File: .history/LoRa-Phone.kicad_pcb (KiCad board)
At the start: 4 copper layers, 60 x 102.5 mm, 188 parts, among them IC1 SKY13373-460LF, IC2 AD8318ACPZ-REEL7, IC3 AD8318ACPZ-REEL7, IC4 TPS2121RUXT, IC5 MAX17048G+T10, IC6 MAX17048G+T10, IC7 TCA9543ADR, IC8 MAX16150AUT+T, J1 Interface, J2 Connector, J3 Connector, J4 BUTTON, J4 JST_MAIN, J6 ROTARY_ENCODER, M1 Motor_DC, Q1 AO3400A, Q4 AO3401A, SW1 POWER, U1 ESP32-S3-WROOM-2, U10 DRV2605LDGS, U11 LC76G, U12 RV-3028-C7, U13 SA818S, U14 INA219BxDCN, U15 INA219BxDCN, U16 INA219BxDCN, U2 TCD-10-23BDX+, U21 WM8960, U23 E22-900M30S, U24 E22-170M30S, U3 MCP23017x-x-ML, U4 BMP390, U5 IS31FL3218-QF, U6 LSM6DSOXTR, U7 BQ24075RGT, U8 MCP23017x-x-ML, U9 BQ24075RGT

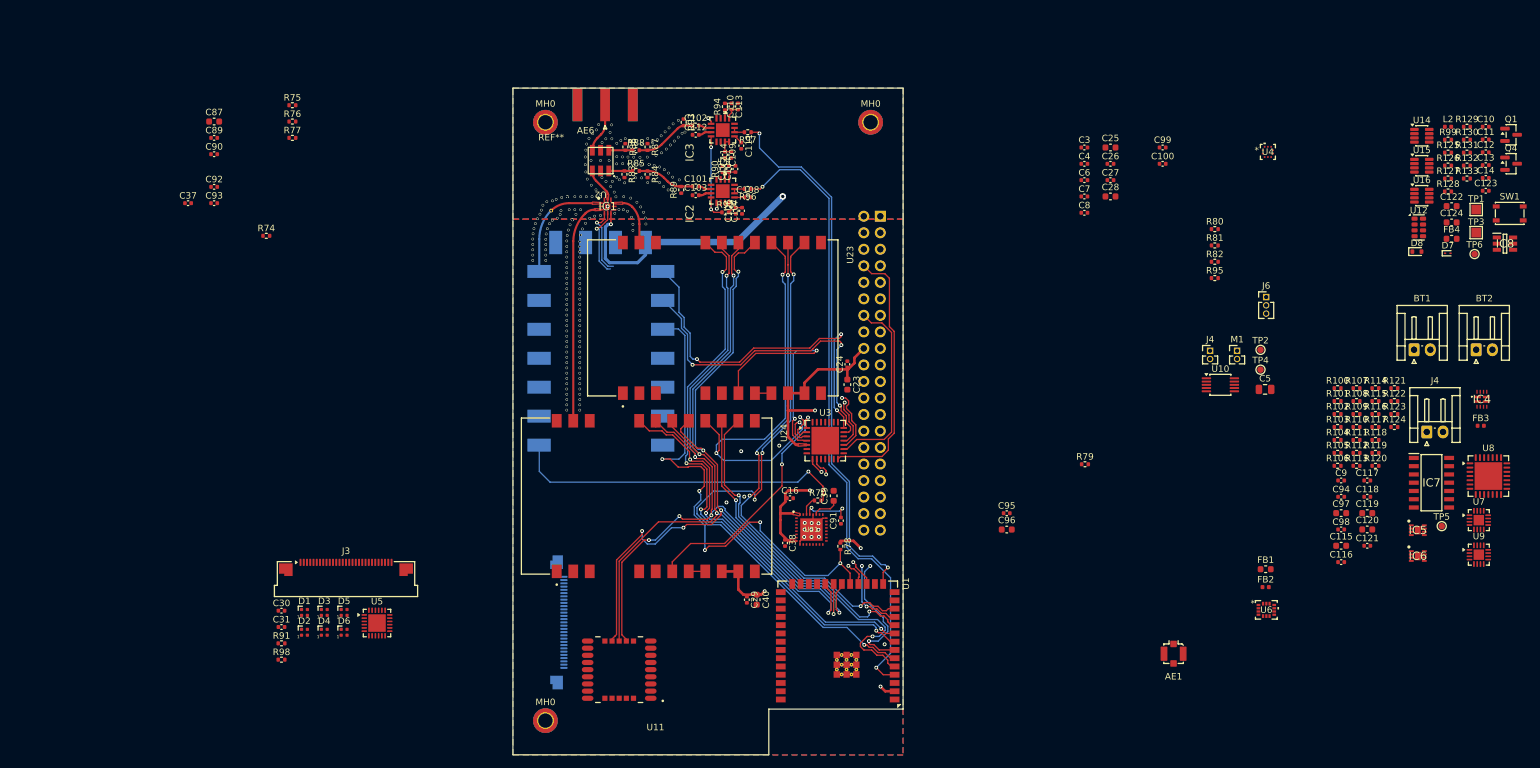
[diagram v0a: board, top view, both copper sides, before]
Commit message: Routed secondary PCB with Power and charging managment, and routed FPC Connector
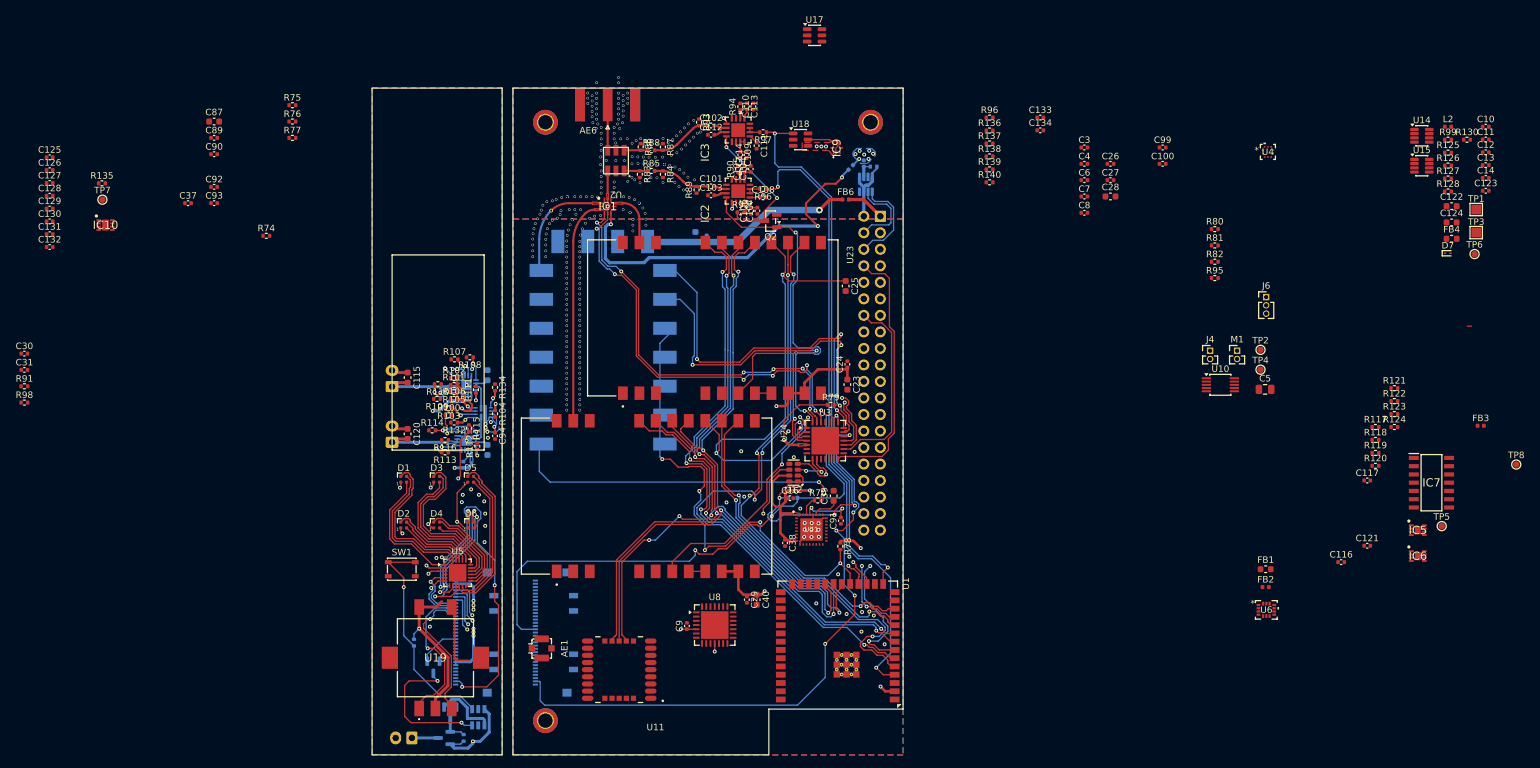
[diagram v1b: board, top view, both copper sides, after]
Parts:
- removed J2: Connector, Connector_FFC-FPC:Amphenol_F32R-1A7x1-11029_1x29-1MP_P0.5mm_Horizontal
- added C125: 100nF, Capacitor_SMD:C_0402_1005Metric, F.Cu at (45.4, 61.9)
- added C126: 2.2uF, Capacitor_SMD:C_0402_1005Metric, F.Cu at (45.4, 63.9)
- added C127: 2.2uF, Capacitor_SMD:C_0402_1005Metric, F.Cu at (45.4, 65.8)
- added C128: 100nF, Capacitor_SMD:C_0402_1005Metric, F.Cu at (45.4, 67.8)
- added C129: 2.2uF, Capacitor_SMD:C_0402_1005Metric, F.Cu at (45.4, 69.8)
- added C130: 100nF, Capacitor_SMD:C_0402_1005Metric, F.Cu at (45.4, 71.7)
- added C131: 100nF, Capacitor_SMD:C_0402_1005Metric, F.Cu at (45.4, 73.7)
- added C132: 100nF, Capacitor_SMD:C_0402_1005Metric, F.Cu at (45.4, 75.7)
- added C133: 100nF, Capacitor_SMD:C_0402_1005Metric, F.Cu at (197.7, 55.8)
- added C134: 100nF, Capacitor_SMD:C_0402_1005Metric, F.Cu at (197.7, 57.7)
- added FB5: 600R @100MHz 500mA, Inductor_SMD:L_0402_1005Metric, B.Cu at (168.5, 63.4)
- added FB6: 600R @100MHz 500mA, Inductor_SMD:L_0402_1005Metric, F.Cu at (167.8, 68.4)
- added FB7: 600R @100MHz 4A, Inductor_SMD:L_0402_1005Metric, B.Cu at (170.6, 62.8)
- added IC10: TPS22965NTDSGRQ1, PTCR:SON50P200X200X80-9N, F.Cu at (54.0, 72.3)
- added IC9: SN74LVC1G74RSE2, PTCR:SN74LVC1G74RSE2, F.Cu at (166.4, 60.4)
- added J5: Board_1, Connector_FFC-FPC:Molex_502244-3330_1x33-1MP_P0.5mm_Horizontal, B.Cu at (110.9, 135.0)
- added Q2: AO3400A, Package_TO_SOT_SMD:SOT-23, F.Cu at (156.2, 71.7)
- added Q3: AO3400A, Package_TO_SOT_SMD:SOT-23, B.Cu at (104.4, 140.3)
- added R134: 5K, Resistor_SMD:R_0402_1005Metric, F.Cu at (113.8, 97.3)
- added R135: 1K, Resistor_SMD:R_0402_1005Metric, F.Cu at (53.4, 65.9)
- added R136: 10K 0.1%, Resistor_SMD:R_0402_1005Metric, F.Cu at (189.9, 57.8)
- added R137: 5.6K 0.1%, Resistor_SMD:R_0402_1005Metric, F.Cu at (189.9, 59.8)
- added R138: 10K 0.1%, Resistor_SMD:R_0402_1005Metric, F.Cu at (189.9, 61.8)
- added R139: 10K, Resistor_SMD:R_0402_1005Metric, F.Cu at (189.9, 63.7)
- added R140: 10K, Resistor_SMD:R_0402_1005Metric, F.Cu at (189.9, 65.7)
- added R96: 10K, Resistor_SMD:R_0402_1005Metric, F.Cu at (189.9, 55.8)
- added TP7: +3V3_RF, TestPoint:TestPoint_Pad_D1.0mm, F.Cu at (53.5, 68.4)
- added TP8: +5V_RF, TestPoint:TestPoint_Pad_D1.0mm, F.Cu at (270.9, 109.1)
- added U17: MCP4725xxx-xCH, Package_TO_SOT_SMD:SOT-23-6, F.Cu at (163.0, 43.1)
- added U18: TLV3501AIDBV, Package_TO_SOT_SMD:SOT-23-6, F.Cu at (160.8, 59.2)
- added U19: RIC11-31S10K2-GSMT, PTCR:RIC1131S10K2GSMT, F.Cu at (104.7, 138.8)
- BT1, BT2, C118, C119, C95, C96, C97, C98, D8, IC4, IC8, J4, Q1, Q4, R129, R131, U16, U7, U9: moved to B.Cu
- FB1: value 600R @100MHz 1A -> 600R @100MHz 2A
- J3: value Connector -> Board_1; footprint Connector_FFC-FPC:Amphenol_F32R-1A7x1-11029_1x29-1MP_P0.5mm_Horizontal -> Connector_FFC-FPC:Molex_502244-3330_1x33-1MP_P0.5mm_Horizontal; moved to B.Cu
- R100: value 13.7K -> 16K
- R101: value 23.7K -> 16K
- R133: value 51.1K -> 100K; moved to B.Cu
- R97: value 1K -> 5.6K 0.1%
- TP5: value +3V3_RF -> +5V_RF
- moved Q4 186.3 mm to (106.0, 151.2), turned to 180 degrees
- moved Q1 185.8 mm to (107.0, 147.4), turned to -90 degrees
- moved R129 180.3 mm to (101.4, 136.5), turned to 90 degrees
- moved SW1 178.9 mm to (99.5, 125.2)
- moved R133 176.6 mm to (109.0, 151.2), turned to -90 degrees
- moved IC8 173.8 mm to (111.3, 148.0), turned to -90 degrees
- moved BT2 167.3 mm to (98.0, 105.7), turned to 90 degrees
- moved J4 163.0 mm to (101.1, 151.2), turned to 180 degrees
- moved R132 160.6 mm to (107.6, 102.7), turned to 180 degrees
- moved BT1 157.2 mm to (98.0, 97.2), turned to 90 degrees
- moved U7 157.0 mm to (109.5, 96.9)
- moved U9 156.6 mm to (109.5, 105.5)
- moved IC4 153.5 mm to (112.1, 101.2), turned to 90 degrees
- moved C120 148.3 mm to (100.4, 104.4), turned to -90 degrees
- moved C115 145.8 mm to (100.4, 95.8), turned to -90 degrees
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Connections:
- C104 pad 1: +3V3_RF -> +5V_RF
- C105 pad 1: +3V3_RF -> +5V_RF
- C106 pad 2: +3V3_RF -> +5V_RF
- C107 pad 2: +3V3_RF -> +5V_RF
- C109 pad 1: +3V3_RF -> +5V_RF
- C110 pad 1: +3V3_RF -> +5V_RF
- C113 pad 2: +3V3_RF -> +5V_RF
- C114 pad 2: +3V3_RF -> +5V_RF
- C123 pad 1: SHUTDOWN -> Net-(IC8-~{CLR})
- C37 pad 1: Net-(U21-DBVDD) -> +3V3
- C95 pad 1: +3V3_RADIO -> +5V_RADIO
- C96 pad 1: +3V3_RADIO -> +5V_RADIO
- D1 pad 1: GND -> +3V3
- D2 pad 1: GND -> +3V3
- D3 pad 1: GND -> +3V3
- D4 pad 1: GND -> +3V3
- D5 pad 1: GND -> +3V3
- D6 pad 1: GND -> +3V3
- D8 pad 1: POWER_BTN -> INT_RTC
- D8 pad 2: INT_RTC -> POWER_BTN_B
- FB3 pad 1: +3V3_RF -> +5V_RF
- FB3 pad 2: +3V3 -> +5V
- IC2 pad 3: +3V3_RF -> +5V_RF
- IC2 pad 4: +3V3_RF -> +5V_RF
- IC2 pad 9: +3V3_RF -> +5V_RF
- IC3 pad 16: AD8318_EN -> Net-(IC3-ENBL)
- IC3 pad 3: +3V3_RF -> +5V_RF
- IC3 pad 4: +3V3_RF -> +5V_RF
- IC3 pad 9: +3V3_RF -> +5V_RF
- IC5 pad 7: SD0 -> SC0
- IC5 pad 8: SC0 -> SD0
- IC6 pad 7: SD1 -> SC1
- IC6 pad 8: SC1 -> SD1
- IC8 pad 1: POWER_BTN -> POWER_BTN_B
- IC8 pad 6: SHUTDOWN -> Net-(IC8-~{CLR})
- J3 pad 10: D5B -> ROT_ENC1
- J3 pad 11: D6R -> ROT_ENC2
- J3 pad 12: D6G -> JOYSTICK_X
- J3 pad 13: D6B -> JOYSTICK_Y
- J3 pad 14: GND -> BUTTON1
- J3 pad 15: GND -> BUTTON0
- J3 pad 16: ROT_ENC2_B -> POWER_BTN
- J3 pad 17: ROT_ENC1_B -> BATS_INT_1
- J3 pad 18: BUTTON0_B -> BAT_SEL_1
- J3 pad 19: D1R -> SHUTDOWN_1
- J3 pad 20: D1G -> BAT_VAL_1
- J3 pad 21: D1B -> BATS_RESET_1
- J3 pad 22: D2R -> GND
- J3 pad 23: D2G -> GND
- J3 pad 24: D2B -> GND
- J3 pad 25: D3R -> +5V
- J3 pad 26: D3G -> +5V
- J3 pad 27: D3B -> +5V
- J3 pad 28: D4R -> GND
- J3 pad 29: D4G -> GND
- J3 pad 3: BUTTON1_B -> +3V3
- J3 pad 4: JOYSTICK_Y_B -> BAT1_PGOOD_1
- J3 pad 5: JOYSTICK_X_B -> BAT1_CHG_1
- J3 pad 6: SDA -> BAT2_PGOOD_1
- J3 pad 7: SCL -> BAT2_CHG_1
- J3 pad 8: D5R -> SDA
- J3 pad 9: D5G -> SCL
- R127 pad 1: +3V3_RADIO -> +3V3_RADIO_OUT
- R128 pad 2: SHUTDOWN -> Net-(IC8-~{CLR})
- R129 pad 1: POWER_BTN -> POWER_BTN_B
- R129 pad 2: BAT_OUT -> +3V3
- R131 pad 1: +3V3 -> Net-(U16-IN-)
- R92 pad 1: AD8318_EN -> Net-(IC3-ENBL)
- R92 pad 2: +3V3_RF -> +5V_RF
- R98 pad 1: SDB -> SDB_1
- SW1 pad 1: POWER_BTN -> POWER_BTN_B
- TP5 pad 1: +3V3_RF -> +5V_RF
- U11 pad 6: BAT_OUT -> unconnected-(U11-V_BCKP-Pad6)
- U13 pad 8: +3V3_RADIO -> +5V_RADIO
- U14 pad 2: +3V3_RADIO -> +3V3_RADIO_OUT
- U16 pad 2: +3V3 -> Net-(U16-IN-)
- U21 pad 10: Net-(U21-DBVDD) -> +3V3
- U23 pad 16: MOSI -> MISO
- U23 pad 17: MISO -> MOSI
- U24 pad 16: MOSI -> MISO
- U24 pad 17: MISO -> MOSI
- U3 pad 16: INTA_MCP -> INTA_MCP_1
- U3 pad 19: SDB -> SDB_1
- U3 pad 22: unconnected-(U3-GPA5-Pad22) -> INT_RTC
- U3 pad 24: INT_RTC -> unconnected-(U3-GPA7-Pad24)
- U5 pad 1: D1R_A -> D1R
- U5 pad 10: D5B_A -> D5G
- U5 pad 11: D5G_A -> D5B
- U5 pad 12: D5R_A -> D5R
- U5 pad 13: D4B_A -> D4G
- U5 pad 14: D4G_A -> D4B
- U5 pad 15: D4R_A -> D4R
- U5 pad 16: D3B_A -> D3G
- U5 pad 17: D3G_A -> D3B
- U5 pad 18: D3R_A -> D3R
- U5 pad 19: D2B_A -> D2G
- U5 pad 20: D2G_A -> D2B
- U5 pad 21: D2R_A -> D2R
- U5 pad 22: D1B_A -> D1G
- U5 pad 23: D1G_A -> D1B
- U5 pad 7: D6B_A -> D6G
- U5 pad 8: D6G_A -> D6B
- U5 pad 9: D6R_A -> D6R
- U8 pad 1: unconnected-(U8-GPB4-Pad1) -> SHDN_COMP
- U8 pad 16: INTA_MCP -> INTA_MCP_2
- U8 pad 17: BAT1_PGOOD -> BAT1_PGOOD_1
- U8 pad 18: BAT1_CHG -> BAT1_CHG_1
- U8 pad 19: BAT2_PGOOD -> BAT2_PGOOD_1
- U8 pad 2: unconnected-(U8-GPB5-Pad2) -> BAT_SEL_1
- U8 pad 20: BAT2_CHG -> BAT2_CHG_1
- U8 pad 21: BATS_INT -> BATS_INT_1
- U8 pad 22: BATS_RESET -> BATS_RESET_1
- U8 pad 23: BAT_VAL -> BAT_VAL_1
- U8 pad 24: BAT_SEL -> unconnected-(U8-GPA7-Pad24)
- U8 pad 26: SHUTDOWN -> SHUTDOWN_1
- U8 pad 27: unconnected-(U8-GPB2-Pad27) -> RF_FAULT
- U8 pad 28: unconnected-(U8-GPB3-Pad28) -> RF_FAULT_RESET
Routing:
- net SDB_1: track 0.00 -> 96.1 mm, vias 0 -> 5
- net POWER_BTN: track 0.00 -> 85.4 mm, vias 0 -> 3
- net RFS_V2: track 10.8 -> 65.4 mm, vias 1 -> 6
- net RFS_V1: track 10.6 -> 62.1 mm, vias 1 -> 6
- net SDB: track 0.00 -> 48.6 mm, vias 0 -> 3
- net INT_RTC: track 0.00 -> 43.4 mm, vias 0 -> 4
- net +3V3: track 50.7 -> 93.2 mm, vias 4 -> 26
- net AD8318_EN: track 14.9 -> 52.9 mm
- net POWER_BTN_B: track 0.00 -> 33.9 mm, vias 0 -> 1
- net +5V_RADIO: track 0.00 -> 33.0 mm, vias 0 -> 1
- net INTA_MCP_1: track 0.00 -> 29.1 mm
- net INTA_MCP: track 29.1 -> 0.00 mm
- net SCL: track 2.62 -> 29.7 mm, vias 1 -> 3
- net SDA: track 3.22 -> 30.2 mm, vias 1 -> 2
- net BAT_OUT: track 0.00 -> 26.5 mm, vias 0 -> 5
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- added copper zone on B.Cu, net +3V3
- added copper zone on B.Cu, net +5V
- added copper zone on B.Cu, net BAT1
- added copper zone on B.Cu, net BAT2
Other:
- board size 60 x 102.5 mm -> 81.6 x 102.5 mm
